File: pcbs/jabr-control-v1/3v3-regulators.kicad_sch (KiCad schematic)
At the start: 25 parts, among them U401 LMQ66430MC3RXBRQ1, U402 TPS7B8133QDRVRQ1, U403 TPS2116DRL

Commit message: Worked on power and other areas of the schematic
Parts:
- removed C408, C409, C410, C411, C412, C413, C414, C415: 4u7, Capacitor_SMD:C_0402_1005Metric, symbol Device:C_Small
- removed TP402, TP403: 1.5mm, TestPoint:TestPoint_Pad_D1.5mm, symbol Connector:TestPoint_Small
- added C1401, C1402, C1403, C1404, C1405, C1406, C1407, C1408: 4u7, project_footprints:C_0402, symbol Device:C_Small
- added TP1401: 1.5mm, TestPoint:TestPoint_Pad_D1.5mm, symbol Connector:TestPoint_Small
- C401, C402: Voltage 50V -> (none)
- C403, C404, C405, C406, C407: footprint Capacitor_SMD:C_0402_1005Metric -> project_footprints:C_0402
- R401: footprint Resistor_SMD:R_0402_1005Metric -> project_footprints:R_0402; now not fitted; now left out of the parts list
- R402, R403: footprint Resistor_SMD:R_0402_1005Metric -> project_footprints:R_0402
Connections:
- net +3V3: no longer C406.1, C407.1, L401.2, R403.2, U401.11 (VOUT/FB)
- net +VIN: no longer C401.1, C402.1, U401.3 (VIN)
- net GND: now also C1401.2, C1402.2, C1403.2, C1404.2, C1405.2, C1406.2, C1407.2, C1408.2
- net 3V3_AON_ST: no longer names the net of U403.8 (ST)
- net EN renamed 3V3_M2_EN
- net MODE renamed 3V3_M2_MODE
- new net +3V3_M2: C1401.1, C1402.1, C1403.1, C1404.1, C1405.1, C1406.1, C1407.1, C1408.1, C406.1, C407.1, L401.2, R403.2, TP1401.1, U401.11 (VOUT/FB)
- new net +5V: C401.1, C402.1, U401.3 (VIN)
- no-connect marks 1 -> 2
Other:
- moved on the sheet: C401, C402, C403, C404, C405, C406, C407, L401, R402, R403, TP401, U401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

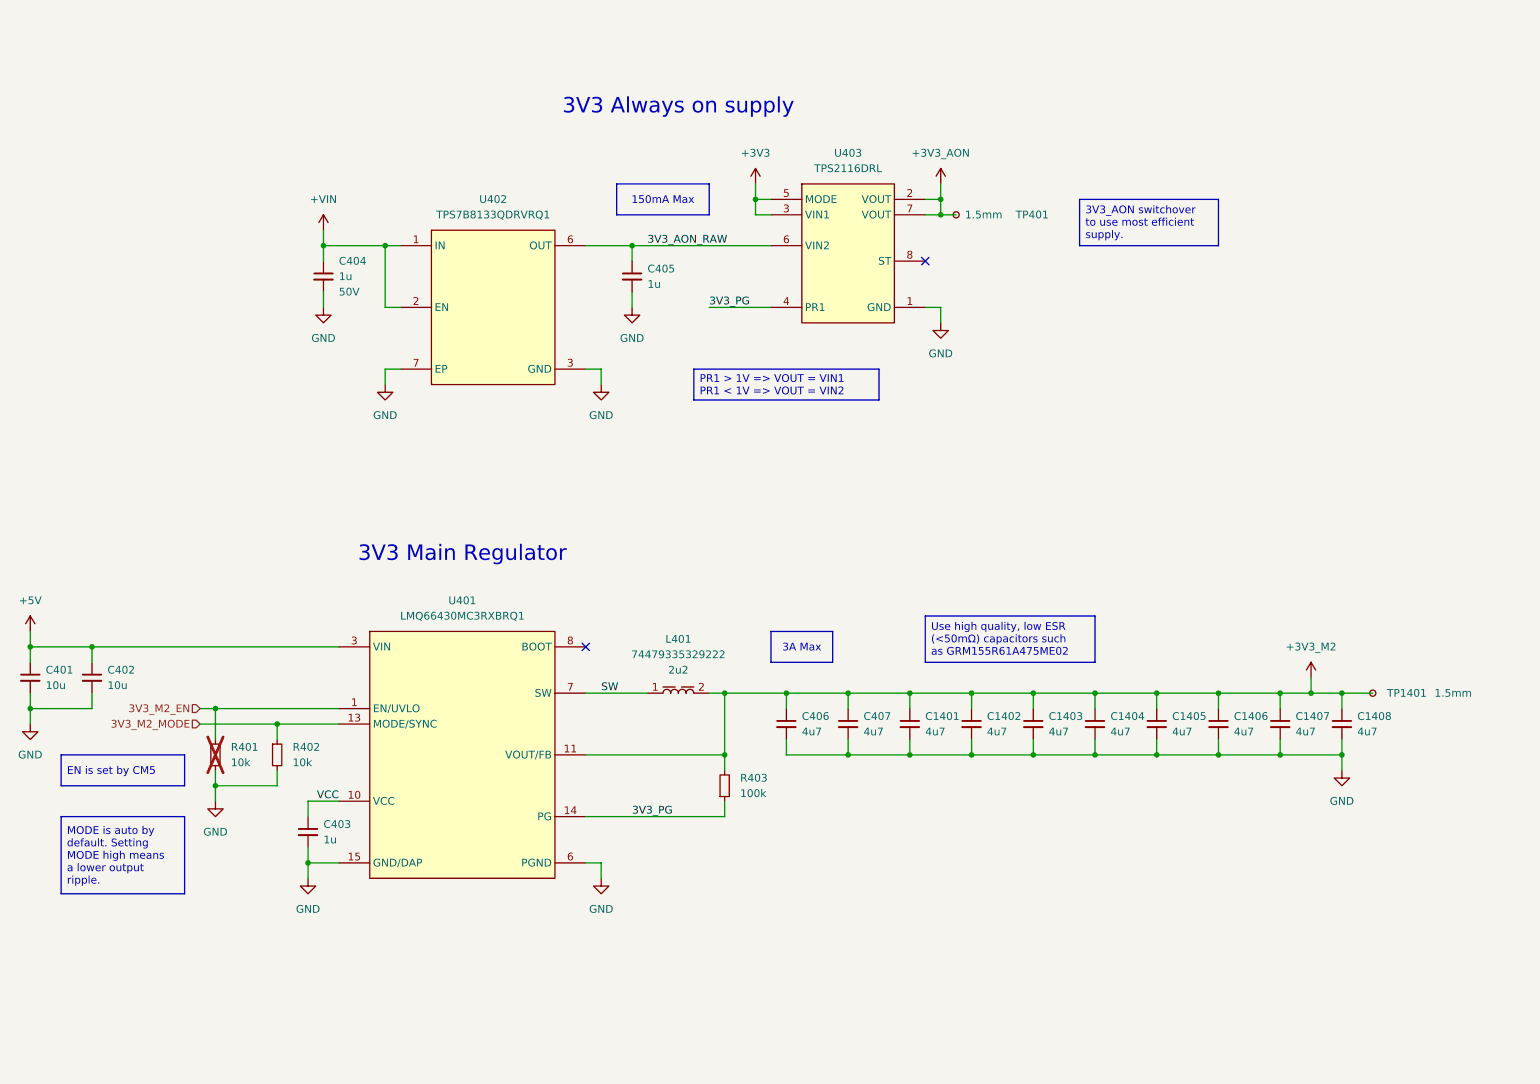
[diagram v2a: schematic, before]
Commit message: Schematic nearing completion, need to do GPIO and PHY decouplings caps
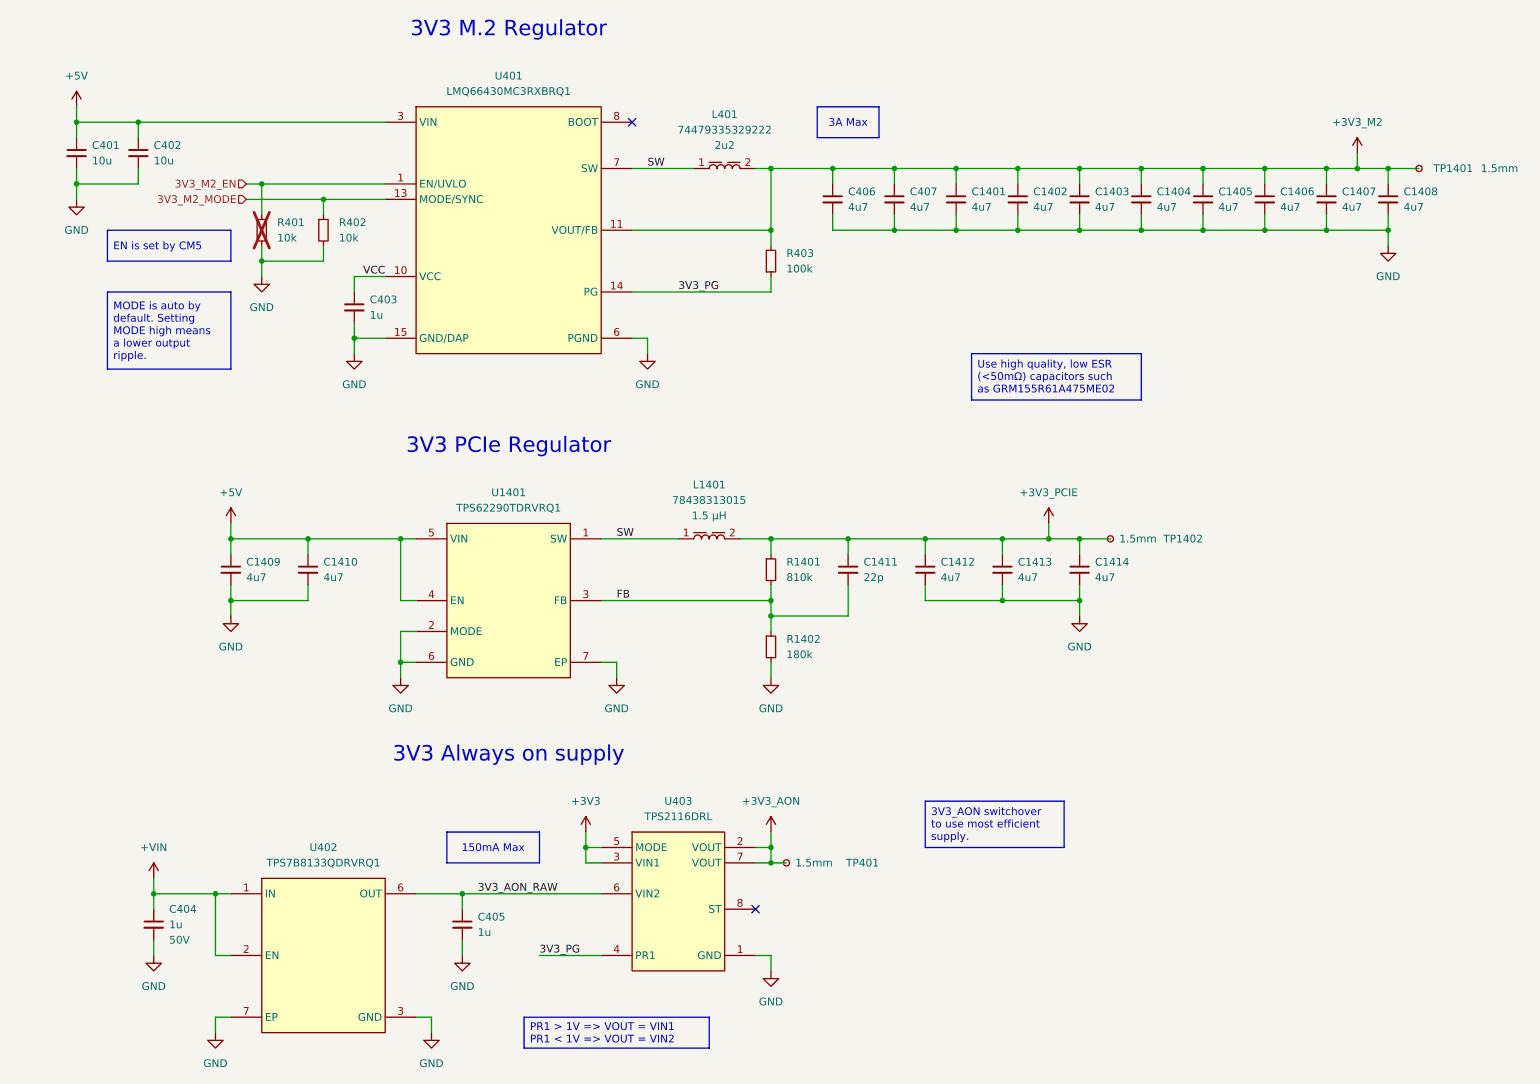
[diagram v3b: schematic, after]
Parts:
- added C1409, C1410, C1412, C1413, C1414: 4u7, project_footprints:C_0402, symbol DEV:C_SMALL
- added C1411: 22p, project_footprints:C_0402, symbol DEV:C_SMALL
- added L1401: 78438313015, project_footprints:L_Wurth_WE-MAIA-1610, symbol PWR-IND:1610_78438313015
- added R1401: 810k, project_footprints:R_0402, symbol Device:R_Small
- added R1402: 180k, project_footprints:R_0402, symbol Device:R_Small
- added TP1402: 1.5mm, project_footprints:TestPoint_Pad_D1.5mm, symbol Connector:TestPoint_Small
- added U1401: TPS62290TDRVRQ1, project_footprints:SON65P200X200X80-7N, symbol PWR-SMPS:TPS62290TDRVRQ1
- C1401, C1402, C1403, C1404, C1405, C1406, C1407, C1408, C403, C404, C405, C406, C407: symbol Device:C_Small -> DEV:C_SMALL
- C401, C402: footprint Capacitor_SMD:C_0805_2012Metric -> project_footprints:C_0805; symbol Device:C_Small -> DEV:C_SMALL
- TP1401: footprint TestPoint:TestPoint_Pad_D1.5mm -> project_footprints:TestPoint_Pad_D1.5mm; now left out of the parts list
- TP401: footprint TestPoint:TestPoint_Pad_D1.5mm -> project_footprints:TestPoint_Pad_D1.5mm
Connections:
- net +5V: now also C1409.1, C1410.1, U1401.4 (EN), U1401.5 (VIN)
- net GND: now also C1409.2, C1410.2, C1412.2, C1413.2, C1414.2, R1402.2, U1401.2 (MODE), U1401.6 (GND), U1401.7 (EP)
- net SW: now also L1401.1, U1401.1 (SW)
- new net +3V3_PCIE: C1411.1, C1412.1, C1413.1, C1414.1, L1401.2, R1401.1, TP1402.1
- new net FB: C1411.2, R1401.2, R1402.1, U1401.3 (FB)
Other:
- note added: "3V3 M.2 Regulator"
- note added: "3V3 PCIe Regulator"
- note removed: "3V3 Main Regulator"
- moved on the sheet: C1401, C1402, C1403, C1404, C1405, C1406, C1407, C1408, C401, C402, C403, C404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
